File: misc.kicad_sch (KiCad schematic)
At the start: 62 parts, among them J1 Serial 1, J10 SW2, J11 SW2, J12 SW2, J13 Rotary Encoder, J14 Paddles, J15 Conn_02x07_Row_Letter_Last, J17 Conn_02x04_Row_Letter_Last, J18 Conn_02x04_Top_Bottom, J19 I2C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

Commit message: Small drawing cleanups.
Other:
- company: (none) -> EZ Electronics
- title: (none) -> Arduino Mega2560 K3NG Keyer - Miscellaneous Circuits
- moved on the sheet: C1, C2, C3, C4, C5, C6, J1, J10, J11, J12, J13, J14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

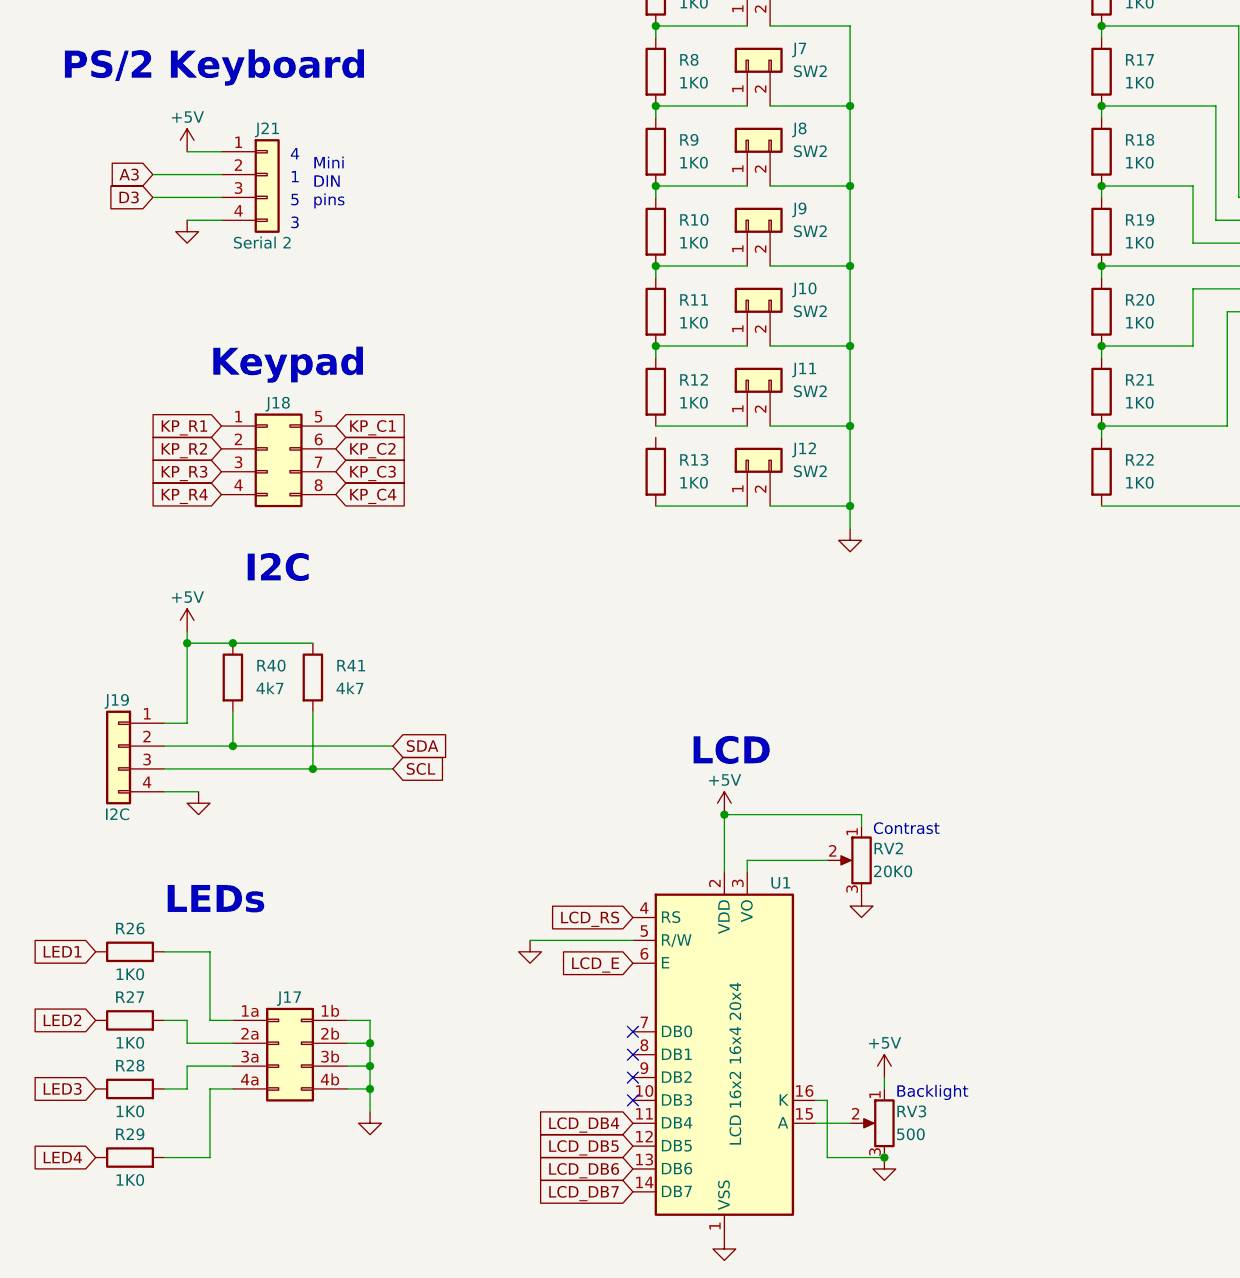
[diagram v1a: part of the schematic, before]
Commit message: Changed power jack and LCD symbols.
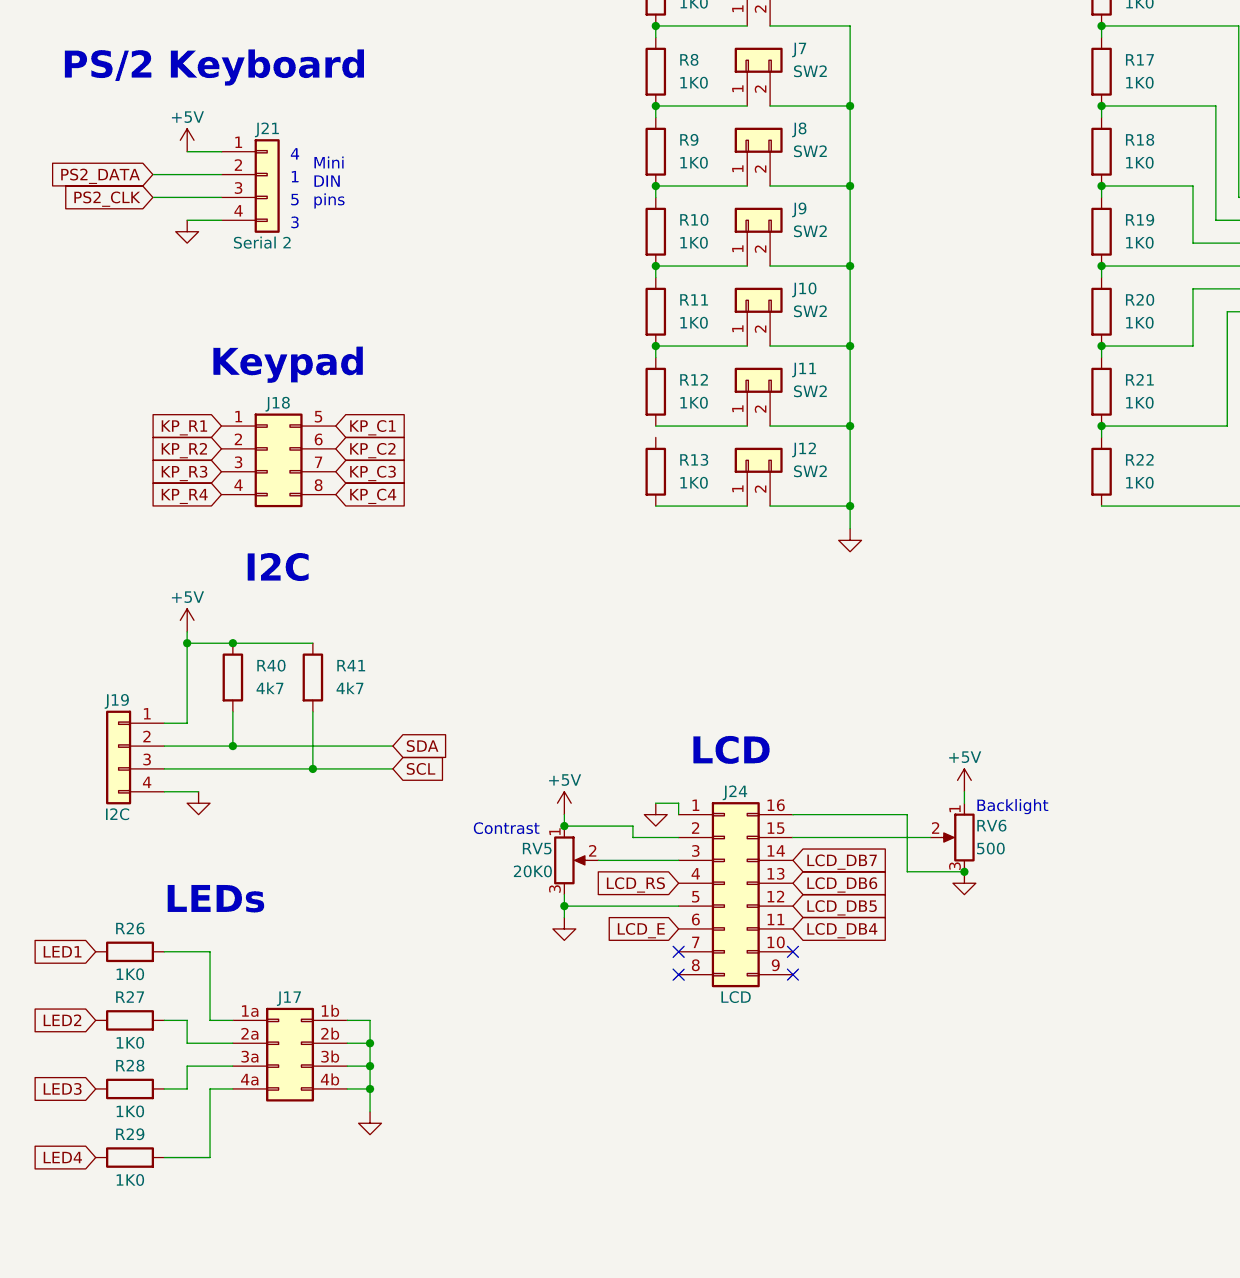
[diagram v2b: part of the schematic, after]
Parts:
- removed RV2: 20K0, symbol Device:R_Potentiometer
- removed RV3: 500, symbol Device:R_Potentiometer
- removed U1: LCD 16x2 16x4 20x4, Display:NHD-0420H1Z, symbol Display_Character:NHD-0420H1Z
- added J24: LCD, symbol Connector_Generic:Conn_02x08_Counter_Clockwise
- added RV5: 20K0, symbol Device:R_Potentiometer
- added RV6: 500, symbol Device:R_Potentiometer
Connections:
- net +5V: now also J24.2 (Pin_2), RV5.1, RV6.1
- net GND: now also J24.1 (Pin_1), J24.16 (Pin_16), J24.5 (Pin_5), RV5.3, RV6.3
- net LCD_DB4: now also J24.11 (Pin_11)
- net LCD_DB5: now also J24.12 (Pin_12)
- net LCD_DB6: now also J24.13 (Pin_13)
- net LCD_DB7: now also J24.14 (Pin_14)
- net LCD_E: now also J24.6 (Pin_6)
- net LCD_RS: now also J24.4 (Pin_4)
- net A3 renamed PS2_DATA
- net D3 renamed PS2_CLK
- new net: J24.3 (Pin_3), RV5.2
- new net: J24.15 (Pin_15), RV6.2
